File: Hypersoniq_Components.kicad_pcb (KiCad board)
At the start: 2 copper layers, 40.4 x 100 mm, 139 parts, among them J1 Conn_01x10_Pin, J2 Conn_01x10_Pin, J3 Conn_01x10_Pin, J4 Eurorack_10_pin_power, U1 TL074, U2 SSI2140, U3 SSI2140, U4 SSI2140, U5 SSI2140, U6 TL072

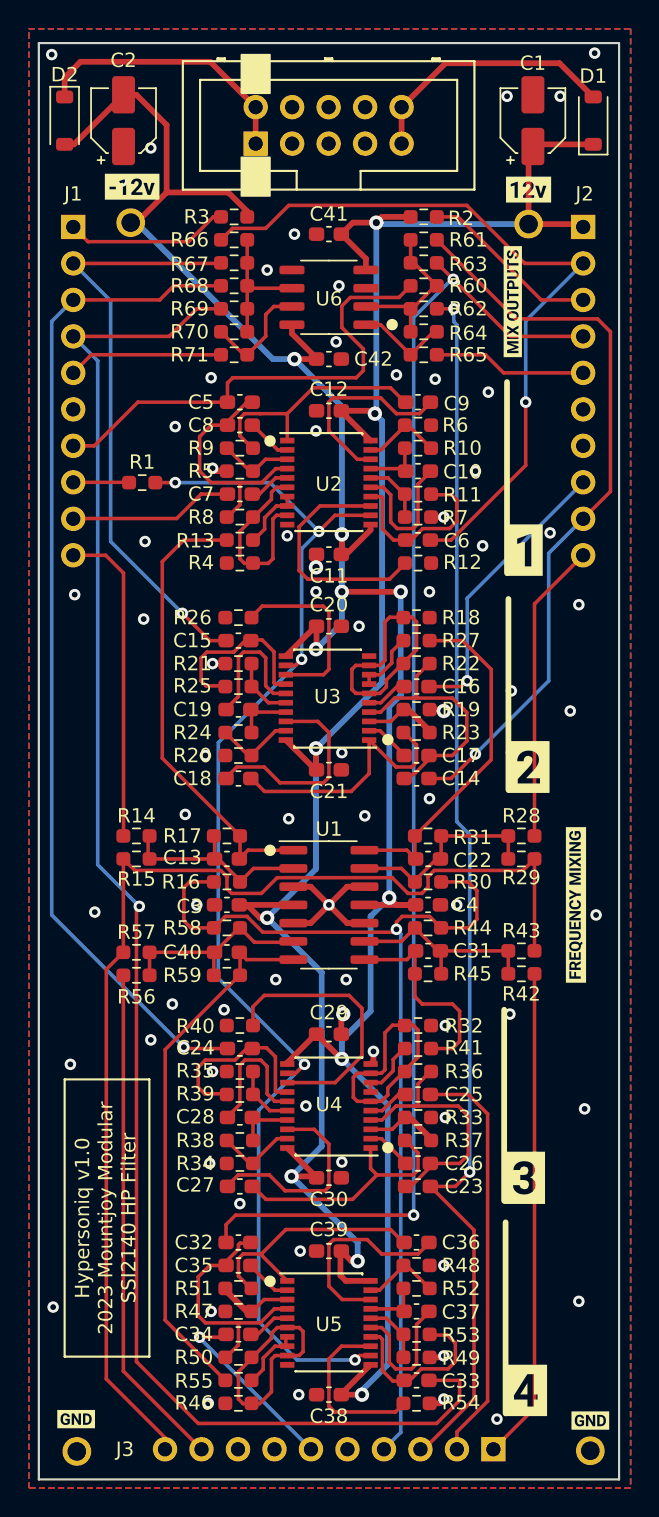
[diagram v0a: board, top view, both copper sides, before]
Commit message: Started generating JLC placement details
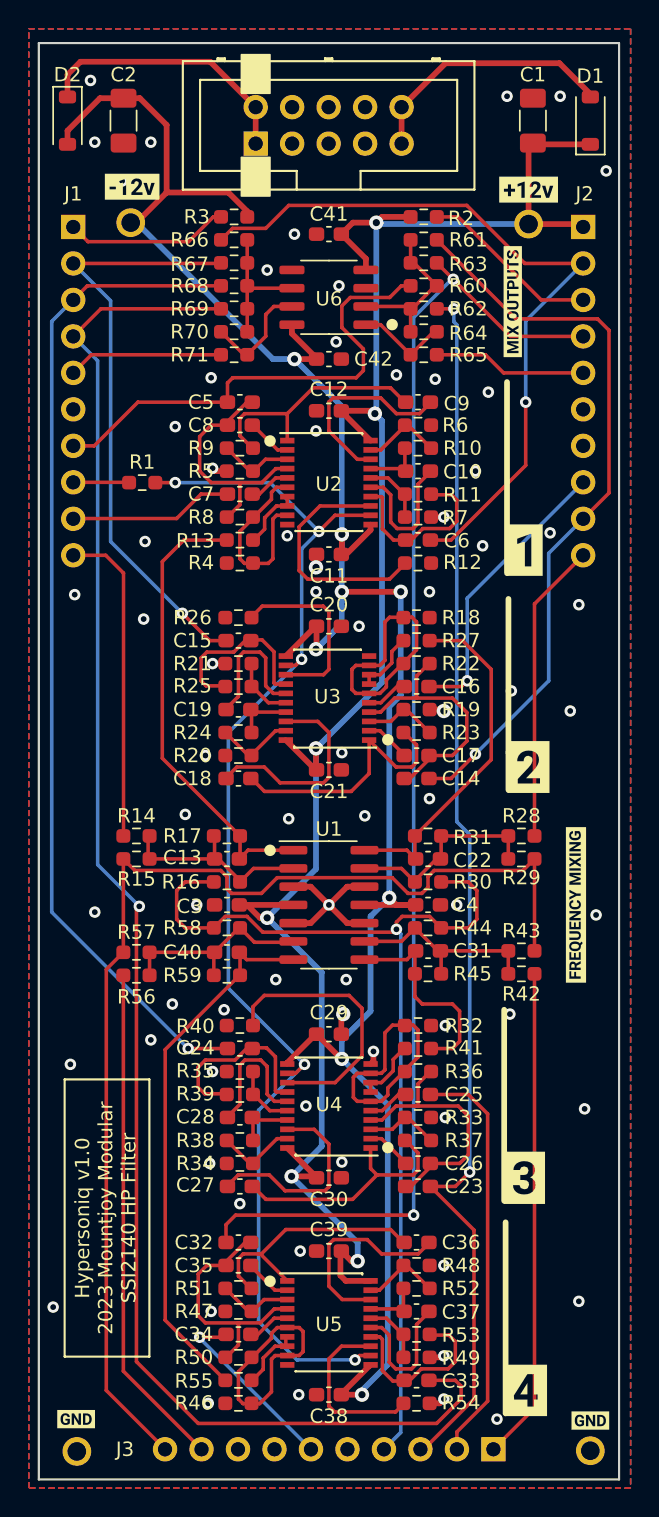
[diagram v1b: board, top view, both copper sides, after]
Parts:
- removed kibuzzard-64BBE4D7: G***, kibuzzard-64BBE4D7
- added kibuzzard-64BE60E0: G***, kibuzzard-64BE60E0, F.Cu at (84.1, 60.2)
- C1, C2: footprint Capacitor_SMD:CP_Elec_4x5.8 -> Capacitor_SMD:C_1206_3216Metric_Pad1.33x1.80mm_HandSolder
- R16, R30, R44, R58: value 50k -> 100k
- moved D2 0.20 mm to (52.0, 55.4)
- moved D1 0.20 mm to (88.4, 55.4)
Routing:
- net Net-(U3-IN2): track 7.84 -> 5.24 mm
- net Net-(U4-IN2): track 7.84 -> 5.24 mm
- net Net-(U5-IN2): track 7.84 -> 5.24 mm
- net /FREQ_POT: track 68.8 -> 69.6 mm
- net /Q_CONTROL: track 90.3 -> 89.8 mm
- net GND: vias 73 -> 74

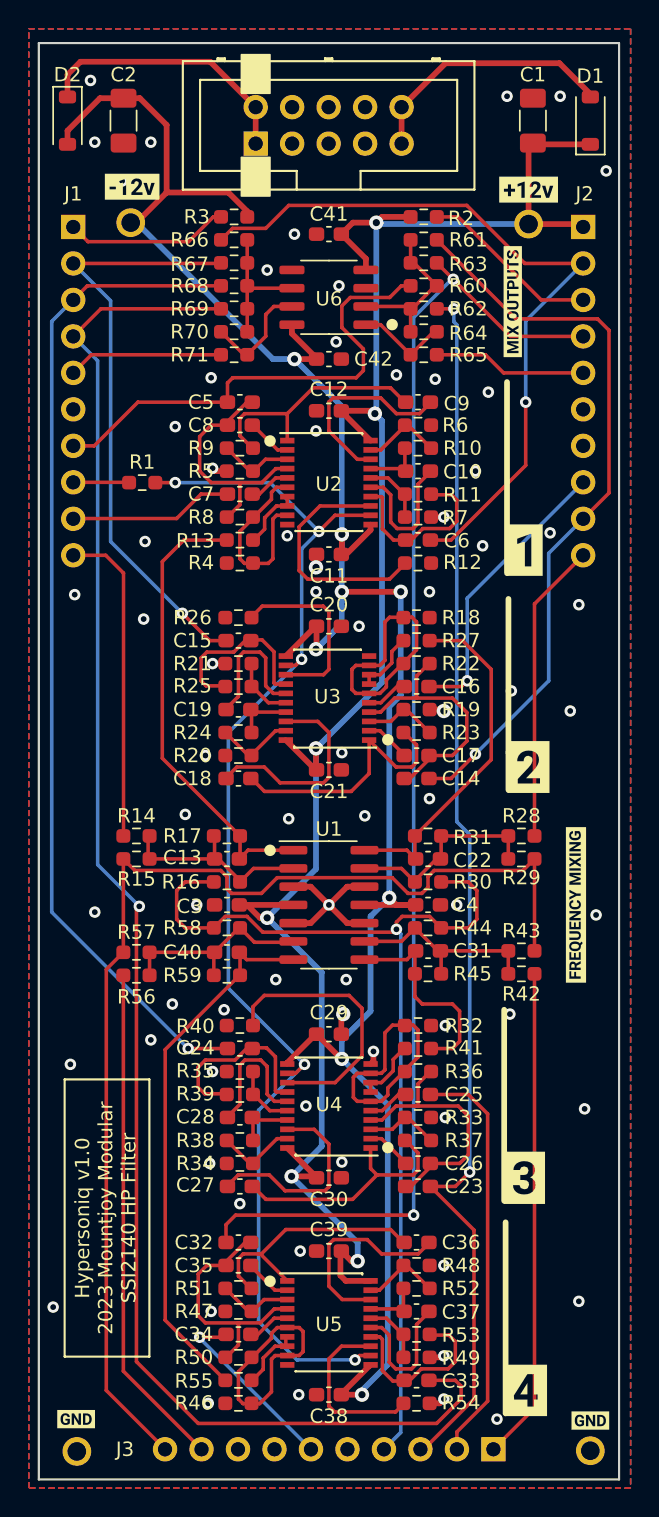
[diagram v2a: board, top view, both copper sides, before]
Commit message: Updated SSI2149 symbol; cleaned up routing on component board
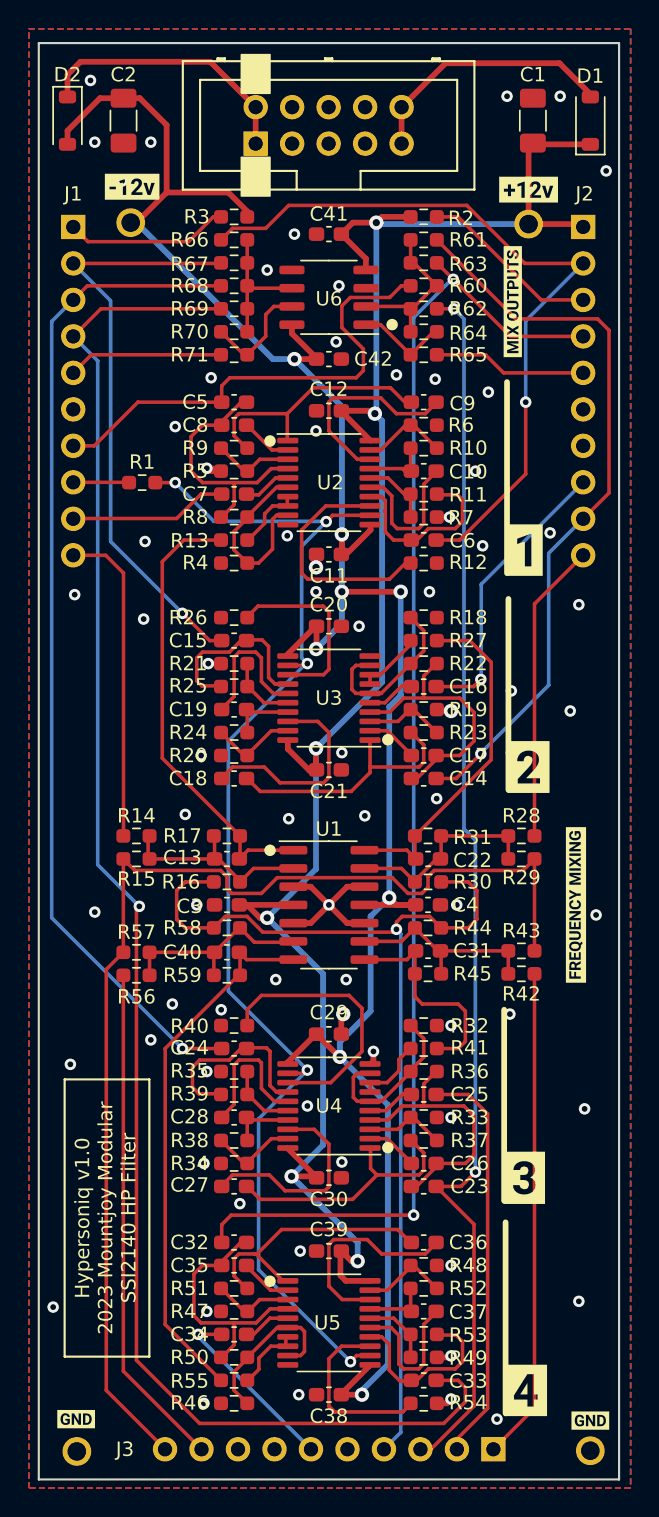
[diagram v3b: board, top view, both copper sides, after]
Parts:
- U2, U3, U4, U5: footprint Package_SO:SSOP-20_4.4x6.5mm_P0.65mm -> Package_SO:TSSOP-20_4.4x6.5mm_P0.65mm
- moved C14 0.50 mm to (76.8, 101.2)
- moved C16 0.50 mm to (76.8, 94.8)
- moved C17 0.50 mm to (76.8, 99.6)
- moved C33 0.50 mm to (76.8, 143.1)
- moved C36 0.50 mm to (76.8, 133.5)
- moved C37 0.50 mm to (76.8, 138.3)
- moved R18 0.50 mm to (76.8, 90.0)
- moved R19 0.50 mm to (76.8, 96.4)
- moved R22 0.50 mm to (76.8, 93.2)
- moved R23 0.50 mm to (76.8, 98.0)
- moved R27 0.50 mm to (76.8, 91.6)
- moved R48 0.50 mm to (76.8, 135.1)
- moved R49 0.50 mm to (76.8, 141.5)
- moved R52 0.50 mm to (76.8, 136.7)
- moved R53 0.50 mm to (76.8, 139.9)
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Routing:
- net /Filter_Voice3/Q_FEEDBACK: track 17.2 -> 11.7 mm
- net /Filter_Voice2/Q_FEEDBACK: track 17.3 -> 11.8 mm
- net /Filter_Voice4/Q_FEEDBACK: track 17.0 -> 11.8 mm
- net GND: track 21.3 -> 20.5 mm
- net /Q_CONTROL: track 89.8 -> 89.0 mm
- net Net-(C5-Pad1): track 16.8 -> 17.6 mm
- net Net-(C36-Pad1): track 18.1 -> 18.9 mm
- net Net-(C27-Pad1): track 17.3 -> 18.1 mm
- net Net-(C37-Pad2): track 9.71 -> 10.3 mm
- net Net-(R48-Pad1): track 5.55 -> 6.09 mm
- net Net-(C36-Pad2): track 13.9 -> 14.4 mm
- net Net-(R54-Pad1): track 12.0 -> 12.5 mm
- net Net-(R49-Pad1): track 4.47 -> 4.97 mm
- net Net-(R19-Pad1): track 5.24 -> 5.74 mm

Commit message: Updated SSI2140 footprints
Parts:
- moved TP3 54.5 mm to (87.9, 93.5)
- moved kibuzzard-640237DF 54.5 mm to (87.9, 91.4)
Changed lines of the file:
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@@
   )
   (footprint "kibuzzard-640237DF" (layer "F.Cu")
-    (at 88.4 145.9)
+    (at 87.9 91.4)
     (descr "Generated with KiBuzzard")
     (tags "kb_params=eyJBbGlnbm1lbnRDaG9pY2UiOiAiQ2VudGVyIiwgIkNhcExlZnRDaG9pY2UiOiAiWyIsICJDYXBSaWdodENob2ljZSI6ICJdIiwgIkZvbnRDb21ib0JveCI6ICJSb2JvdG8tQm9sZCIsICJIZWlnaHRDdHJsIjogIi43IiwgIkxheWVyQ29tYm9Cb3giOiAiRi5TaWxrUyIsICJNdWx0aUxpbmVUZXh0IjogIkdORCIsICJQYWRkaW5nQm90dG9tQ3RybCI6ICI1IiwgIlBhZGRpbmdMZWZ0Q3RybCI6ICI1IiwgIlBhZGRpbmdSaWdodEN0cmwiOiAiNSIsICJQYWRkaW5nVG9wQ3RybCI6ICI1IiwgIldpZHRoQ3RybCI6ICIifQ==")
@@
   )
   (footprint "Custom_Footprints:1.3mm_Test_Point" (layer "F.Cu")
-    (at 88.4 148)
+    (at 87.9 93.5)
     (descr "1.3mm Test Point")
     (tags "Through Hole Mount Test Points")
@@
   (via (at 69.3 86.5) (size 1) (drill 0.5) (layers "F.Cu" "B.Cu") (net 2))
   (via (at 70.2 110) (size 0.8) (drill 0.4) (layers "F.Cu" "B.Cu") (free) (net 2))
-  (via (at 53.6 52.6) (size 0.8) (drill 0.4) (layers "F.Cu" "B.Cu") (free) (net 2))
+  (via (at 53.8 52.6) (size 0.8) (drill 0.4) (layers "F.Cu" "B.Cu") (free) (net 2))
   (via (at 61 110) (size 0.8) (drill 0.4) (layers "F.Cu" "B.Cu") (free) (net 2))
   (via (at 72.7 103.8) (size 0.8) (drill 0.4) (layers "F.Cu" "B.Cu") (free) (net 2))
@@
   (segment (start 68.5 139.7) (end 68.5 141.1) (width 0.25) (layer "F.Cu") (net 37))
   (segment (start 66.6 139.425) (end 68.225 139.425) (width 0.25) (layer "F.Cu") (net 37))
+  (segment (start 78.32 51.4) (end 86.9 51.4) (width 0.4) (layer "F.Cu") (net 38))
   (segment (start 75.26 54.46) (end 75.26 57) (width 0.4) (layer "F.Cu") (net 38))
+  (segment (start 88.4 52.9) (end 88.4 53.75) (width 0.4) (layer "F.Cu") (net 38))
+  (segment (start 86.9 51.4) (end 88.4 52.9) (width 0.4) (layer "F.Cu") (net 38))
   (segment (start 75.26 54.46) (end 78.32 51.4) (width 0.4) (layer "F.Cu") (net 38))
-  (segment (start 86.25 51.4) (end 88.4 53.55) (width 0.4) (layer "F.Cu") (net 38))
-  (segment (start 88.4 53.55) (end 88.4 53.75) (width 0.4) (layer "F.Cu") (net 38))
-  (segment (start 78.32 51.4) (end 86.25 51.4) (width 0.4) (layer "F.Cu") (net 38))
   (segment (start 65.1 54.46) (end 61.94 51.3) (width 0.4) (layer "F.Cu") (net 39))
-  (segment (start 61.94 51.3) (end 52.9 51.3) (width 0.4) (layer "F.Cu") (net 39))
-  (segment (start 52 52.2) (end 52 53.75) (width 0.4) (layer "F.Cu") (net 39))
+  (segment (start 52 52.5) (end 52 53.75) (width 0.4) (layer "F.Cu") (net 39))
+  (segment (start 61.94 51.3) (end 53.2 51.3) (width 0.4) (layer "F.Cu") (net 39))
   (segment (start 65.1 54.46) (end 65.1 57) (width 0.4) (layer "F.Cu") (net 39))
-  (segment (start 52.9 51.3) (end 52 52.2) (width 0.4) (layer "F.Cu") (net 39))
+  (segment (start 53.2 51.3) (end 52 52.5) (width 0.4) (layer "F.Cu") (net 39))
   (segment (start 55.8875 142.4575) (end 61.33 147.9) (width 0.25) (layer "F.Cu") (net 40))
   (segment (start 55.8875 114.9) (end 55.8875 142.4575) (width 0.25) (layer "F.Cu") (net 40))

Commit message: v1.0 Design sent for manufacture
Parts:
- moved C41 8.70 mm to (70.2, 72.0), turned to 0 degrees
- moved C42 8.70 mm to (70.2, 63.3), turned to 180 degrees
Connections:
- J3 pad 5: GND -> -12V
- U6 pad 4: +12V -> -12V
- U6 pad 8: -12V -> +12V
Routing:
- net -12V: track 154.3 -> 176.1 mm
- net +12V: track 139.5 -> 143.2 mm, vias 6 -> 7
